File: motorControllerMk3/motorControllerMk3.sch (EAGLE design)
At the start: 41 parts, among them J1 AVR_SPI_PRG_6NS

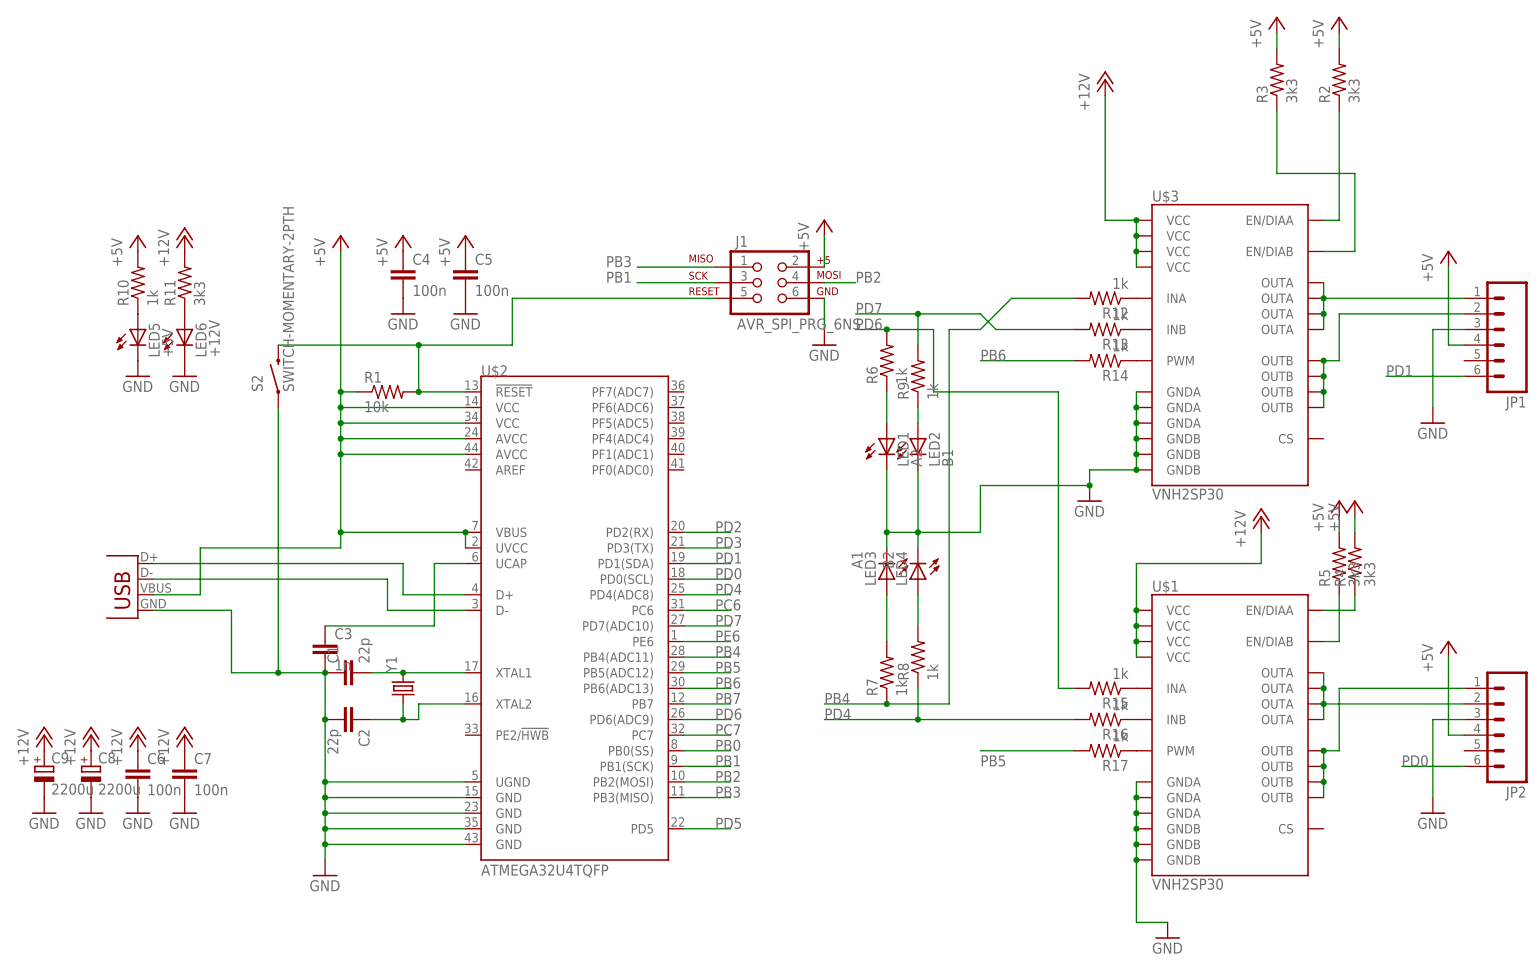
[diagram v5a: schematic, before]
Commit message: fixed mistakes in layout, added usb resistors
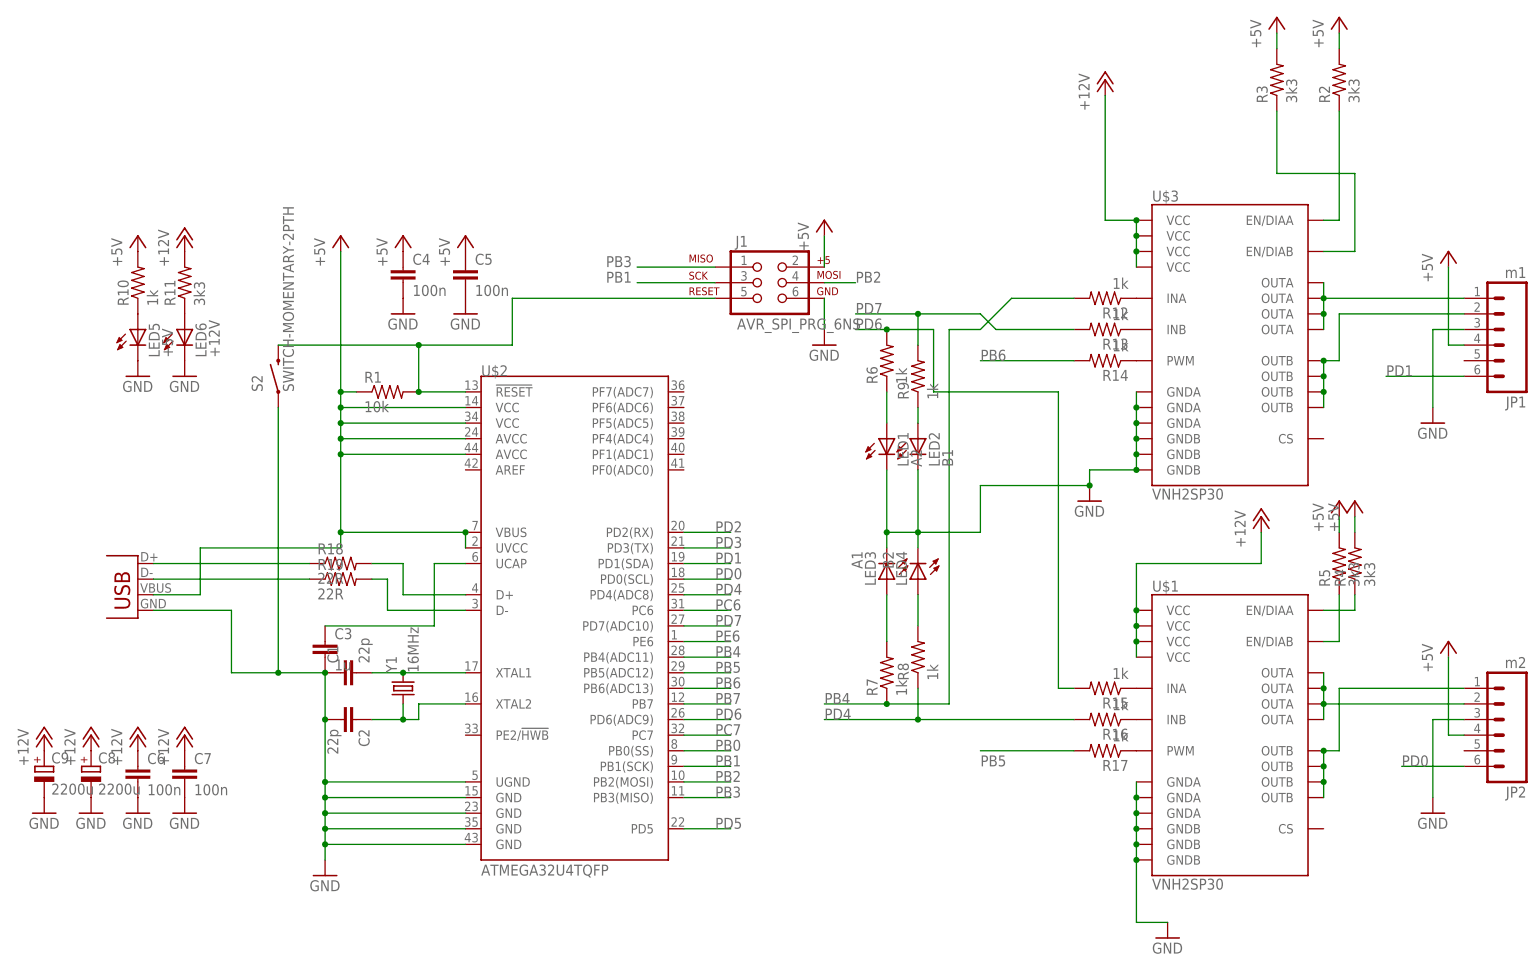
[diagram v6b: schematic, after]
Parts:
- added R18, R19: 22R, SparkFun-Passives:RESISTOR0805-RES
- C3: value 1n -> 1u
- JP1: value (none) -> m1
- JP2: value (none) -> m2
- Y1: value (none) -> 16MHz
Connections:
- new net N$14: JP3.D+, R18.1
- new net N$15: JP3.D-, R19.1
- net N$10: now also R18.2; no longer JP3.D+
- net N$11: now also R19.2; no longer JP3.D-
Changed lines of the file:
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@@
 <part name="C1" library="SparkFun-Passives" deviceset="CAP" device="0805" value="22p"/>
 <part name="C2" library="SparkFun-Passives" deviceset="CAP" device="0805" value="22p"/>
-<part name="C3" library="SparkFun-Passives" deviceset="CAP" device="0805" value="1n"/>
+<part name="C3" library="SparkFun-Passives" deviceset="CAP" device="0805" value="1u"/>
 <part name="C4" library="SparkFun-Passives" deviceset="CAP" device="0805" value="100n"/>
 <part name="C5" library="SparkFun-Passives" deviceset="CAP" device="0805" value="100n"/>
@@
 <part name="P+18" library="supply1" deviceset="+12V" device=""/>
 <part name="GND14" library="supply1" deviceset="GND" device=""/>
-<part name="JP1" library="SparkFun-Connectors" deviceset="M06" device="SIP"/>
-<part name="JP2" library="SparkFun-Connectors" deviceset="M06" device="SIP"/>
+<part name="JP1" library="SparkFun-Connectors" deviceset="M06" device="SIP" value="m1"/>
+<part name="JP2" library="SparkFun-Connectors" deviceset="M06" device="SIP" value="m2"/>
 <part name="U$2" library="SparkFun-DigitalIC" deviceset="ATMEGA32U4" device="TQFP"/>
 <part name="S2" library="SparkFun-Electromechanical" deviceset="SWITCH-MOMENTARY-2" device="PTH"/>
-<part name="Y1" library="SparkFun-FreqCtrl" deviceset="CRYSTAL" device="HC49US"/>
+<part name="Y1" library="SparkFun-FreqCtrl" deviceset="CRYSTAL" device="HC49US" value="16MHz"/>
 <part name="U$1" library="SparkFun-PowerIC" deviceset="VNH2SP30" device=""/>
 <part name="U$3" library="SparkFun-PowerIC" deviceset="VNH2SP30" device=""/>
 <part name="J1" library="SparkFun-Connectors" deviceset="AVR_SPI_PRG_6" device="NS"/>
 <part name="JP3" library="SparkFun-Connectors" deviceset="USB" device="-SMD-NS"/>
+<part name="R18" library="SparkFun-Passives" deviceset="RESISTOR" device="0805-RES" value="22R"/>
+<part name="R19" library="SparkFun-Passives" deviceset="RESISTOR" device="0805-RES" value="22R"/>
 </parts>
 <sheets>
@@
 <instance part="J1" gate="G$1" x="38.1" y="104.14"/>
 <instance part="JP3" gate="G$1" x="-63.5" y="50.8" rot="MR0"/>
+<instance part="R18" gate="G$1" x="-30.48" y="58.42"/>
+<instance part="R19" gate="G$1" x="-30.48" y="55.88"/>
 </instances>
 <busses>
@@
 <net name="N$10" class="0">
 <segment>
-<wire x1="-60.96" y1="58.42" x2="-20.32" y2="58.42" width="0.1524" layer="91"/>
 <wire x1="-20.32" y1="58.42" x2="-20.32" y2="53.34" width="0.1524" layer="91"/>
 <pinref part="U$2" gate="G$1" pin="D+"/>
 <wire x1="-20.32" y1="53.34" x2="-10.16" y2="53.34" width="0.1524" layer="91"/>
-<pinref part="JP3" gate="G$1" pin="D+"/>
+<pinref part="R18" gate="G$1" pin="2"/>
+<wire x1="-25.4" y1="58.42" x2="-20.32" y2="58.42" width="0.1524" layer="91"/>
 </segment>
 </net>
 <net name="N$11" class="0">
 <segment>
-<wire x1="-22.86" y1="55.88" x2="-60.96" y2="55.88" width="0.1524" layer="91"/>
 <wire x1="-22.86" y1="55.88" x2="-22.86" y2="50.8" width="0.1524" layer="91"/>
 <pinref part="U$2" gate="G$1" pin="D-"/>
 <wire x1="-22.86" y1="50.8" x2="-10.16" y2="50.8" width="0.1524" layer="91"/>
-<pinref part="JP3" gate="G$1" pin="D-"/>
+<pinref part="R19" gate="G$1" pin="2"/>
+<wire x1="-22.86" y1="55.88" x2="-25.4" y2="55.88" width="0.1524" layer="91"/>
 </segment>
 </net>
@@
 </segment>
 </net>
+<net name="N$14" class="0">
+<segment>
+<pinref part="JP3" gate="G$1" pin="D+"/>
+<pinref part="R18" gate="G$1" pin="1"/>
+<wire x1="-60.96" y1="58.42" x2="-35.56" y2="58.42" width="0.1524" layer="91"/>
+</segment>
+</net>
+<net name="N$15" class="0">
+<segment>
+<pinref part="R19" gate="G$1" pin="1"/>
+<pinref part="JP3" gate="G$1" pin="D-"/>
+<wire x1="-35.56" y1="55.88" x2="-60.96" y2="55.88" width="0.1524" layer="91"/>
+</segment>
+</net>
 </nets>
 </sheet>
 </sheets>
+<errors>
+</errors>
 </schematic>
 </drawing>

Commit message: turned around some resistors to get better silkscreen
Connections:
- removed net N$27: LED3.A, R7.2
- removed net N$31: LED1.A, R6.1
- new net N$16: LED3.A, R7.1
- new net N$18: LED1.A, R6.2
- net PB4: now also R7.2; no longer R7.1
- net PD6: now also R6.1; no longer R6.2
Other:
- moved on the sheet: R6, R7
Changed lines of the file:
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@@
 <instance part="LED3" gate="G$1" x="58.42" y="55.88" rot="R180"/>
 <instance part="LED4" gate="G$1" x="63.5" y="55.88" rot="R180"/>
-<instance part="R6" gate="G$1" x="58.42" y="91.44" rot="R90"/>
-<instance part="R7" gate="G$1" x="58.42" y="40.64" rot="R90"/>
+<instance part="R6" gate="G$1" x="58.42" y="88.9" rot="MR270"/>
+<instance part="R7" gate="G$1" x="58.42" y="40.64" rot="MR270"/>
 <instance part="R8" gate="G$1" x="63.5" y="43.18" rot="R90"/>
 <instance part="R9" gate="G$1" x="63.5" y="88.9" rot="R90"/>
@@
 <net name="PB4" class="0">
 <segment>
-<pinref part="R7" gate="G$1" pin="1"/>
 <wire x1="68.58" y1="96.52" x2="68.58" y2="35.56" width="0.1524" layer="91"/>
-<wire x1="68.58" y1="35.56" x2="58.42" y2="35.56" width="0.1524" layer="91"/>
 <wire x1="68.58" y1="96.52" x2="73.66" y2="96.52" width="0.1524" layer="91"/>
 <wire x1="73.66" y1="96.52" x2="78.74" y2="101.6" width="0.1524" layer="91"/>
 <pinref part="R12" gate="G$1" pin="2"/>
 <wire x1="78.74" y1="101.6" x2="88.9" y2="101.6" width="0.1524" layer="91"/>
+<label x="48.26" y="35.56" size="1.778" layer="95"/>
+<pinref part="R7" gate="G$1" pin="2"/>
+<wire x1="68.58" y1="35.56" x2="58.42" y2="35.56" width="0.1524" layer="91"/>
 <wire x1="58.42" y1="35.56" x2="48.26" y2="35.56" width="0.1524" layer="91"/>
 <junction x="58.42" y="35.56"/>
-<label x="48.26" y="35.56" size="1.778" layer="95"/>
 </segment>
 <segment>
@@
 <net name="PD6" class="0">
 <segment>
-<wire x1="58.42" y1="96.52" x2="53.34" y2="96.52" width="0.1524" layer="91"/>
-<pinref part="R6" gate="G$1" pin="2"/>
 <pinref part="R15" gate="G$1" pin="2"/>
 <wire x1="88.9" y1="38.1" x2="86.36" y2="38.1" width="0.1524" layer="91"/>
@@
 <wire x1="86.36" y1="86.36" x2="66.04" y2="86.36" width="0.1524" layer="91"/>
 <wire x1="66.04" y1="86.36" x2="66.04" y2="96.52" width="0.1524" layer="91"/>
+<label x="53.34" y="96.52" size="1.778" layer="95"/>
+<pinref part="R6" gate="G$1" pin="1"/>
 <wire x1="66.04" y1="96.52" x2="58.42" y2="96.52" width="0.1524" layer="91"/>
+<wire x1="58.42" y1="96.52" x2="58.42" y2="93.98" width="0.1524" layer="91"/>
+<wire x1="58.42" y1="96.52" x2="53.34" y2="96.52" width="0.1524" layer="91"/>
 <junction x="58.42" y="96.52"/>
-<label x="53.34" y="96.52" size="1.778" layer="95"/>
 </segment>
 <segment>
@@
 </segment>
 </net>
-<net name="N$27" class="0">
-<segment>
-<pinref part="LED3" gate="G$1" pin="A"/>
-<pinref part="R7" gate="G$1" pin="2"/>
-<wire x1="58.42" y1="53.34" x2="58.42" y2="45.72" width="0.1524" layer="91"/>
-</segment>
-</net>
 <net name="N$30" class="0">
 <segment>
@@
 <pinref part="R9" gate="G$1" pin="1"/>
 <wire x1="63.5" y1="81.28" x2="63.5" y2="83.82" width="0.1524" layer="91"/>
-</segment>
-</net>
-<net name="N$31" class="0">
-<segment>
-<pinref part="LED1" gate="G$1" pin="A"/>
-<pinref part="R6" gate="G$1" pin="1"/>
-<wire x1="58.42" y1="81.28" x2="58.42" y2="86.36" width="0.1524" layer="91"/>
 </segment>
 </net>
@@
 </segment>
 </net>
+<net name="N$16" class="0">
+<segment>
+<pinref part="R7" gate="G$1" pin="1"/>
+<pinref part="LED3" gate="G$1" pin="A"/>
+<wire x1="58.42" y1="45.72" x2="58.42" y2="53.34" width="0.1524" layer="91"/>
+</segment>
+</net>
+<net name="N$18" class="0">
+<segment>
+<pinref part="LED1" gate="G$1" pin="A"/>
+<pinref part="R6" gate="G$1" pin="2"/>
+<wire x1="58.42" y1="81.28" x2="58.42" y2="83.82" width="0.1524" layer="91"/>
+</segment>
+</net>

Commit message: bla
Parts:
- added C10: 100n, SparkFun-Passives:CAP0805
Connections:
- net +5V: now also C10.1
- net GND: now also C10.2
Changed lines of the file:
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@@
 <part name="R18" library="SparkFun-Passives" deviceset="RESISTOR" device="0805-RES" value="22R"/>
 <part name="R19" library="SparkFun-Passives" deviceset="RESISTOR" device="0805-RES" value="22R"/>
+<part name="C10" library="SparkFun-Passives" deviceset="CAP" device="0805" value="100n"/>
+<part name="P+19" library="supply1" deviceset="+5V" device=""/>
+<part name="GND15" library="supply1" deviceset="GND" device=""/>
 </parts>
 <sheets>
@@
 <instance part="R18" gate="G$1" x="-30.48" y="58.42"/>
 <instance part="R19" gate="G$1" x="-30.48" y="55.88"/>
+<instance part="C10" gate="G$1" x="-48.26" y="22.86"/>
+<instance part="P+19" gate="1" x="-48.26" y="30.48"/>
+<instance part="GND15" gate="1" x="-48.26" y="17.78"/>
 </instances>
 <busses>
@@
 <pinref part="R10" gate="G$1" pin="2"/>
 <pinref part="P+15" gate="1" pin="+5V"/>
+</segment>
+<segment>
+<pinref part="C10" gate="G$1" pin="1"/>
+<pinref part="P+19" gate="1" pin="+5V"/>
 </segment>
 </net>
@@
 <wire x1="99.06" y1="0" x2="104.14" y2="0" width="0.1524" layer="91"/>
 </segment>
+<segment>
+<pinref part="C10" gate="G$1" pin="2"/>
+<pinref part="GND15" gate="1" pin="GND"/>
+</segment>
 </net>
